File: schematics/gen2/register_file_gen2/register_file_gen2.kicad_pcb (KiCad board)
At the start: 2 copper layers, 100.1 x 91.1 mm, 15 parts, among them U1 74LS02, U2 74LS02

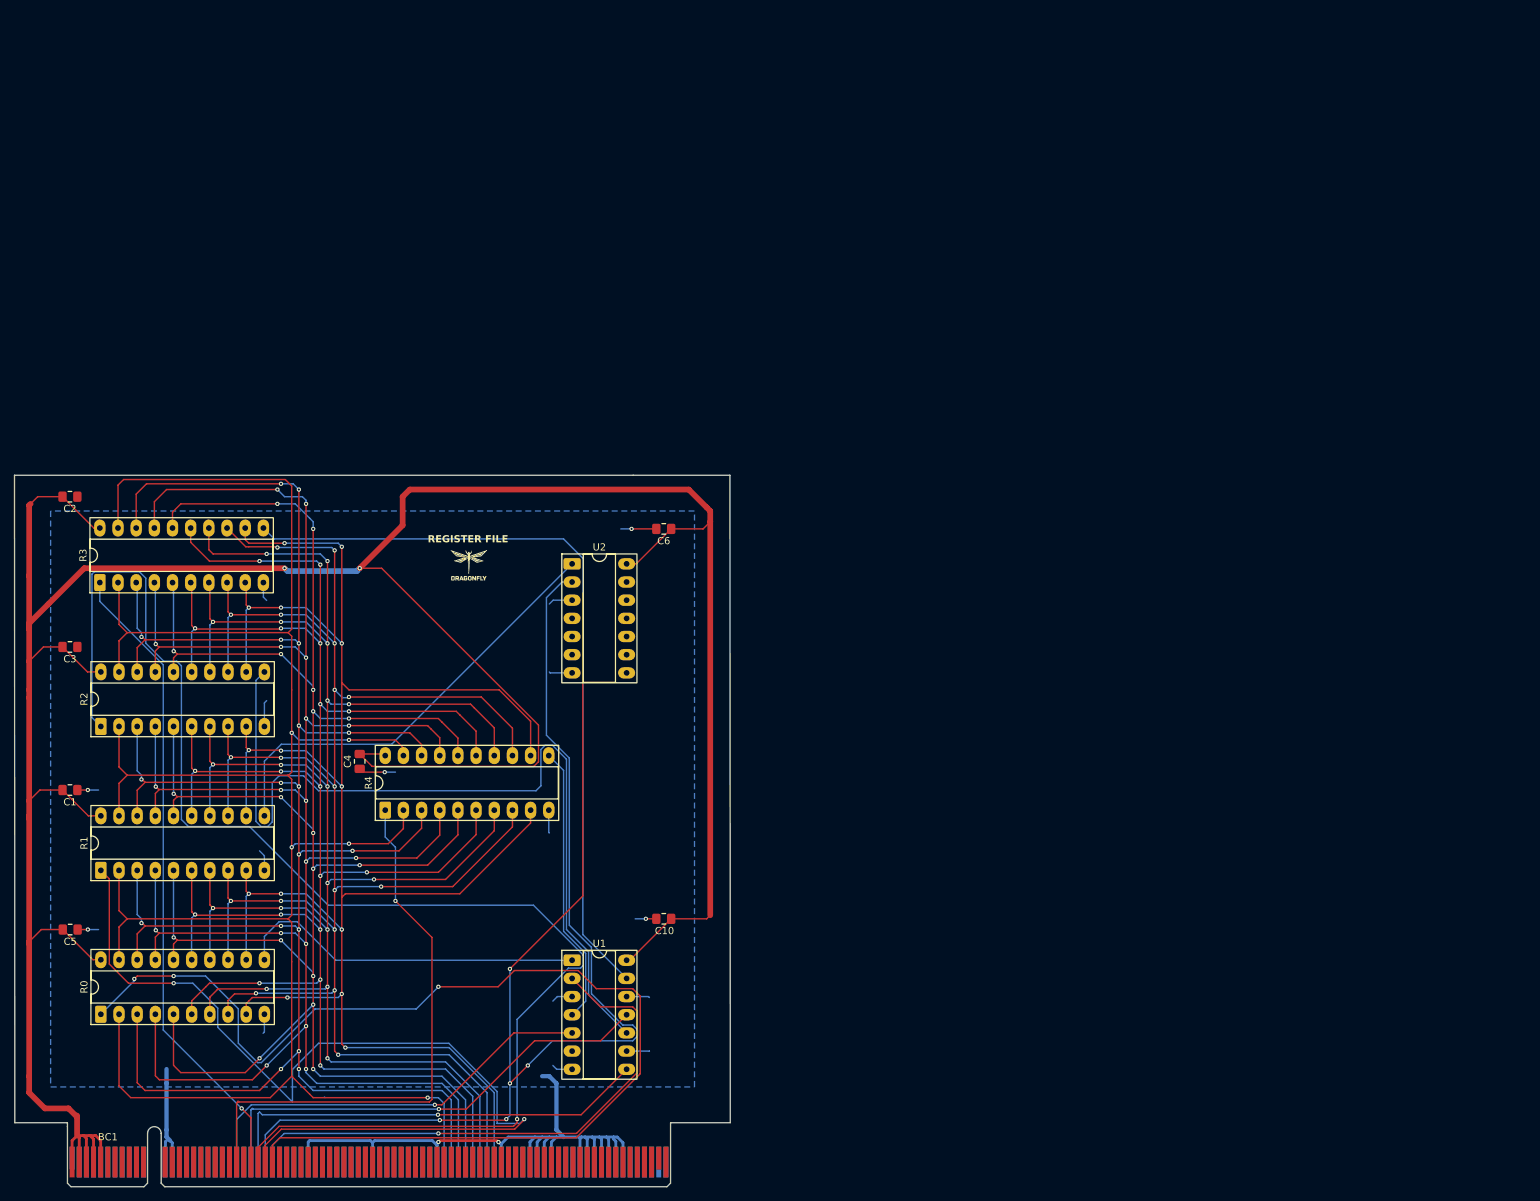
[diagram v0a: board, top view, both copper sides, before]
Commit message: remake of register file module
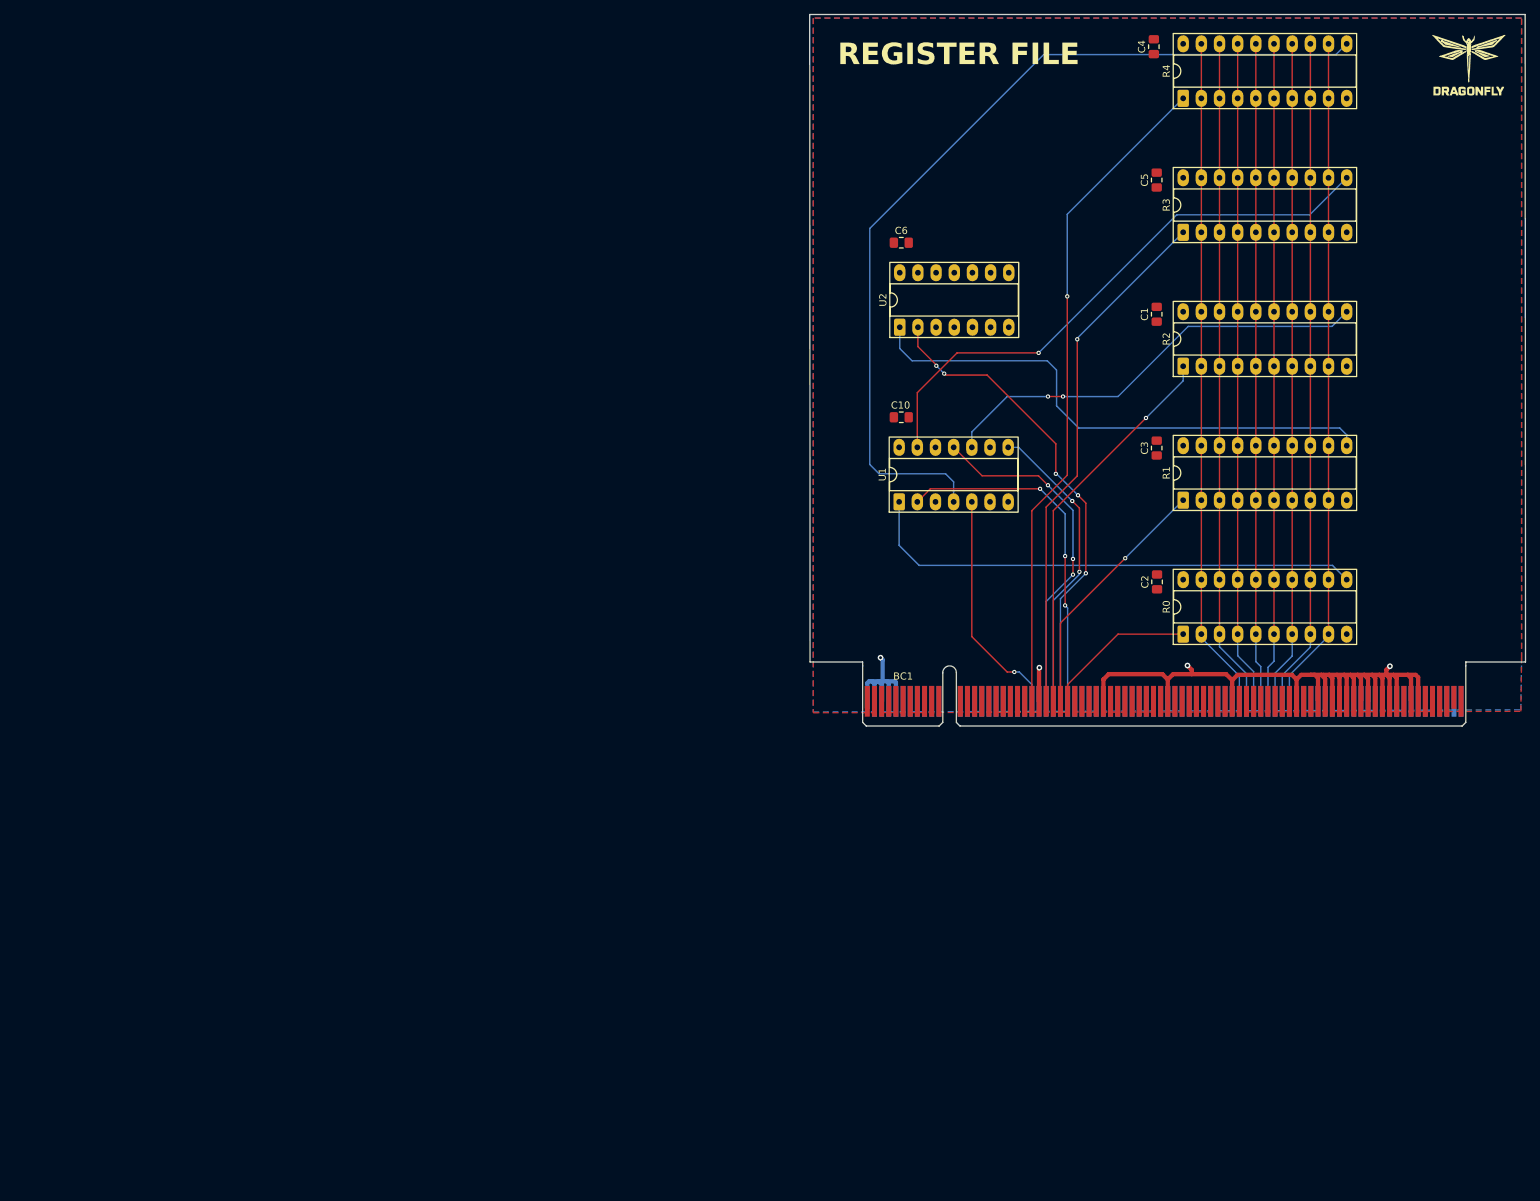
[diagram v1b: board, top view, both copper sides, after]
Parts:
- moved C5 184.5 mm to (233.4, 35.2), turned to 90 degrees
- moved C1 165.8 mm to (233.4, 54.0), turned to 90 degrees
- moved R0 160.3 mm to (237.1, 98.7)
- moved R1 159.9 mm to (237.1, 80.0)
- moved R2 159.4 mm to (237.1, 61.3)
- moved R3 159.1 mm to (237.1, 42.5)
- moved C3 154.4 mm to (233.4, 72.7), turned to 90 degrees
- moved C2 152.4 mm to (233.4, 91.4), turned to 90 degrees
- moved R4 149.5 mm to (237.1, 23.8)
- moved C4 149.3 mm to (233.0, 16.6)
- moved BC1 128.5 mm to (192.9, 108.1)
- moved U1 78.7 mm to (197.4, 80.2), turned to 90 degrees
- moved C10 77.6 mm to (197.7, 68.4), turned to 0 degrees
- moved U2 56.5 mm to (197.5, 55.8), turned to 90 degrees
- moved C6 52.0 mm to (197.7, 44.0), turned to 0 degrees
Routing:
- net VCC: track 421.9 -> 21.1 mm, vias 2 -> 1
- net /D0: track 326.6 -> 94.1 mm, vias 5 -> 0
- net /D1: track 323.1 -> 93.5 mm, vias 18 -> 0
- net /D2: track 319.0 -> 92.8 mm, vias 18 -> 0
- net /D3: track 314.4 -> 92.2 mm, vias 18 -> 0
- net /D4: track 292.3 -> 92.3 mm, vias 18 -> 0
- net /D5: track 290.2 -> 92.9 mm, vias 18 -> 0
- net /D6: track 286.2 -> 93.5 mm, vias 18 -> 0
- net /D7: track 283.8 -> 94.2 mm, vias 14 -> 0
- net Net-(BC1-~{RYH}): track 198.6 -> 54.4 mm
- net Net-(BC1-~{LZL}): track 208.8 -> 66.9 mm
- net Net-(BC1-~{RZH}): track 161.1 -> 21.4 mm, vias 3 -> 0
- net Net-(BC1-~{RZL}): track 134.8 -> 35.2 mm, vias 2 -> 1
- net Net-(R4-Cp): track 39.1 -> 125.9 mm
- net Net-(R2-Cp): track 120.3 -> 61.5 mm, vias 0 -> 2
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- added copper zone on F.Cu, net VCC
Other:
- board size 100.1 x 91.1 mm -> 100 x 91.1 mm

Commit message: fixed errors
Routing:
- net GND: track 120.4 -> 173.1 mm, vias 3 -> 5
